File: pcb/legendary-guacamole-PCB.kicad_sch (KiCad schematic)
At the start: 2 parts

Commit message: forget to commit
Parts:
- added U1: nRF52840, Package_DFN_QFN:Nordic_AQFN-73-1EP_7x7mm_P0.5mm, symbol MCU_Nordic:nRF52840
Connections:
- new net: U1.A22 (VDD), U1.AD14 (VDD), U1.AD23 (VDD), U1.B1 (VDD), U1.W1 (VDD)
- new net: U1.B7 (VSS), U1.EP (VSS)
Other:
- note removed: "Columns"
- note removed: "Rows"

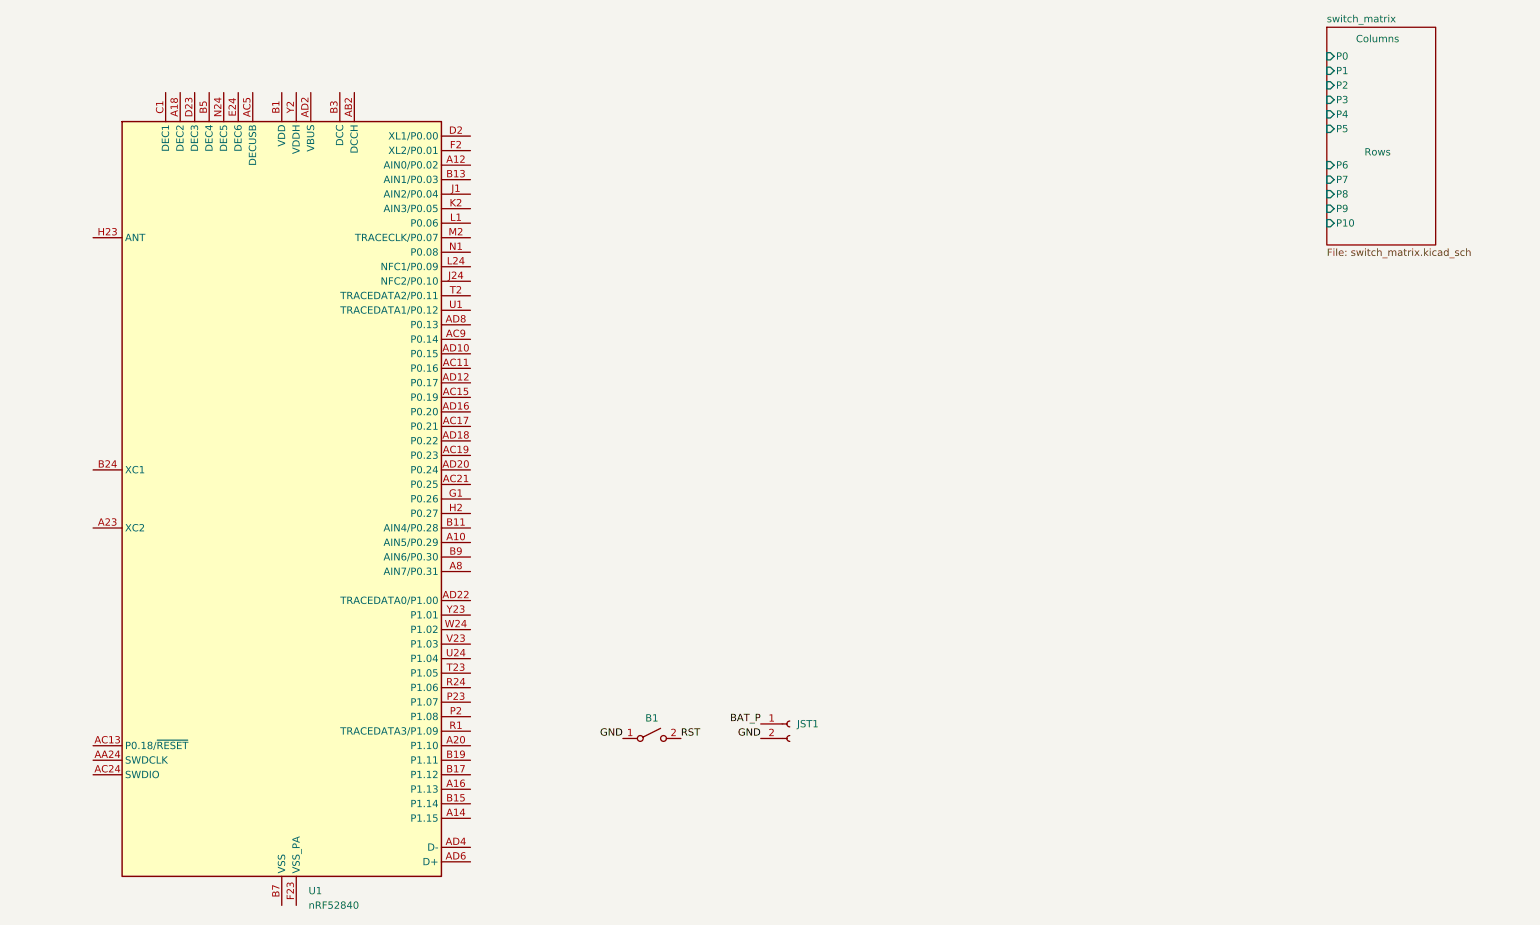
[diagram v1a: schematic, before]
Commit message: fix diff between updated pcb and schematic
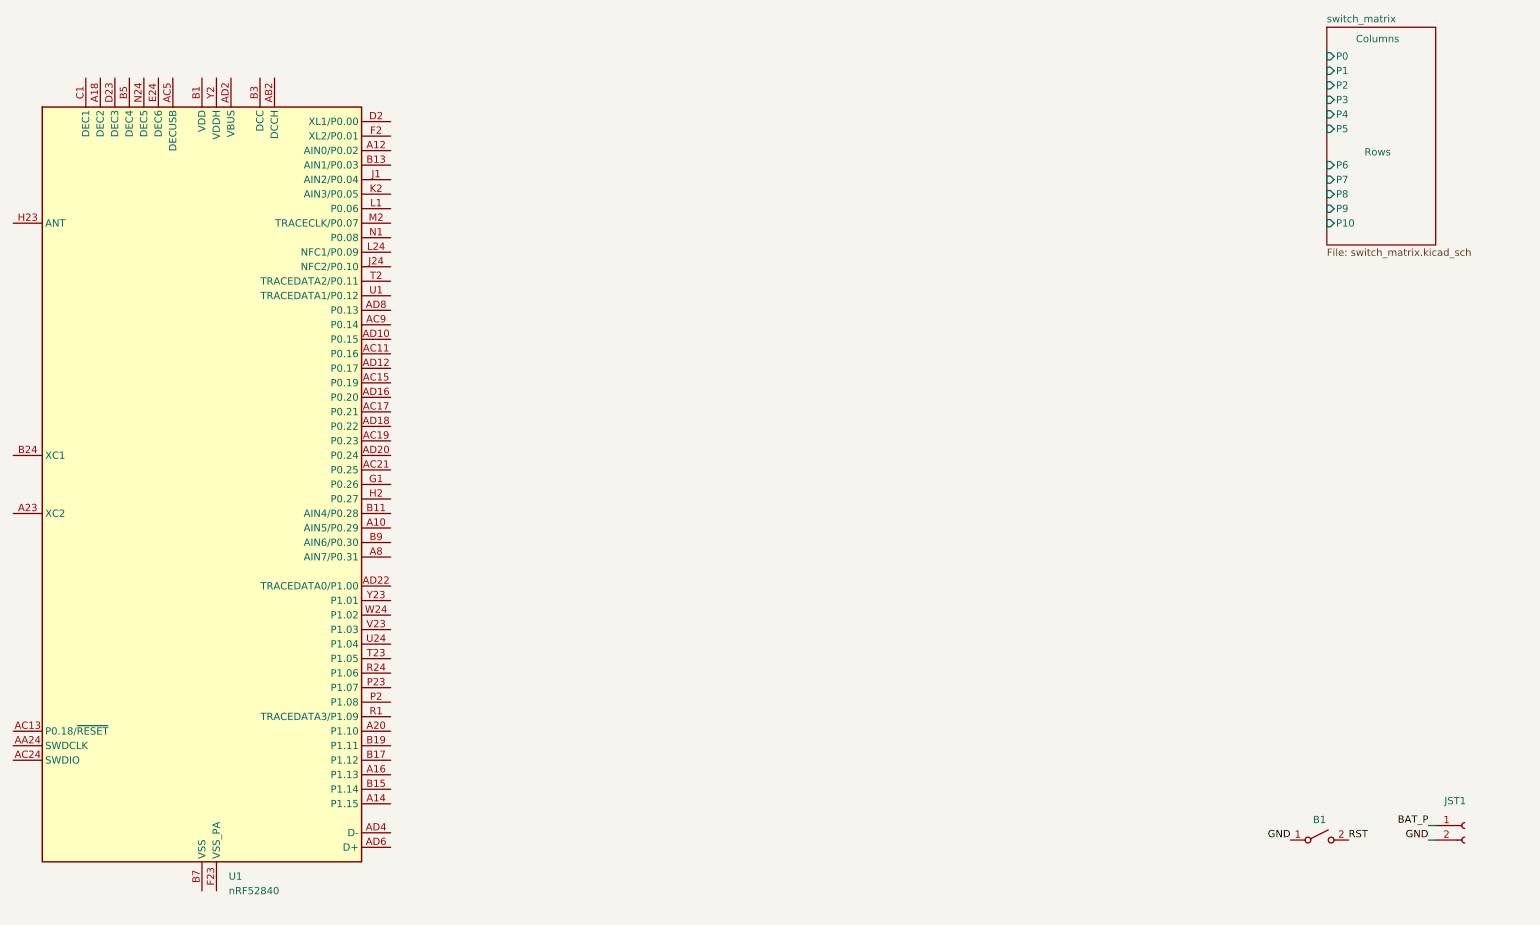
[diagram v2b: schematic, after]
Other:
- moved on the sheet: B1, JST1, U1

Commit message: finish pcb routing, generate fabrication file and bom
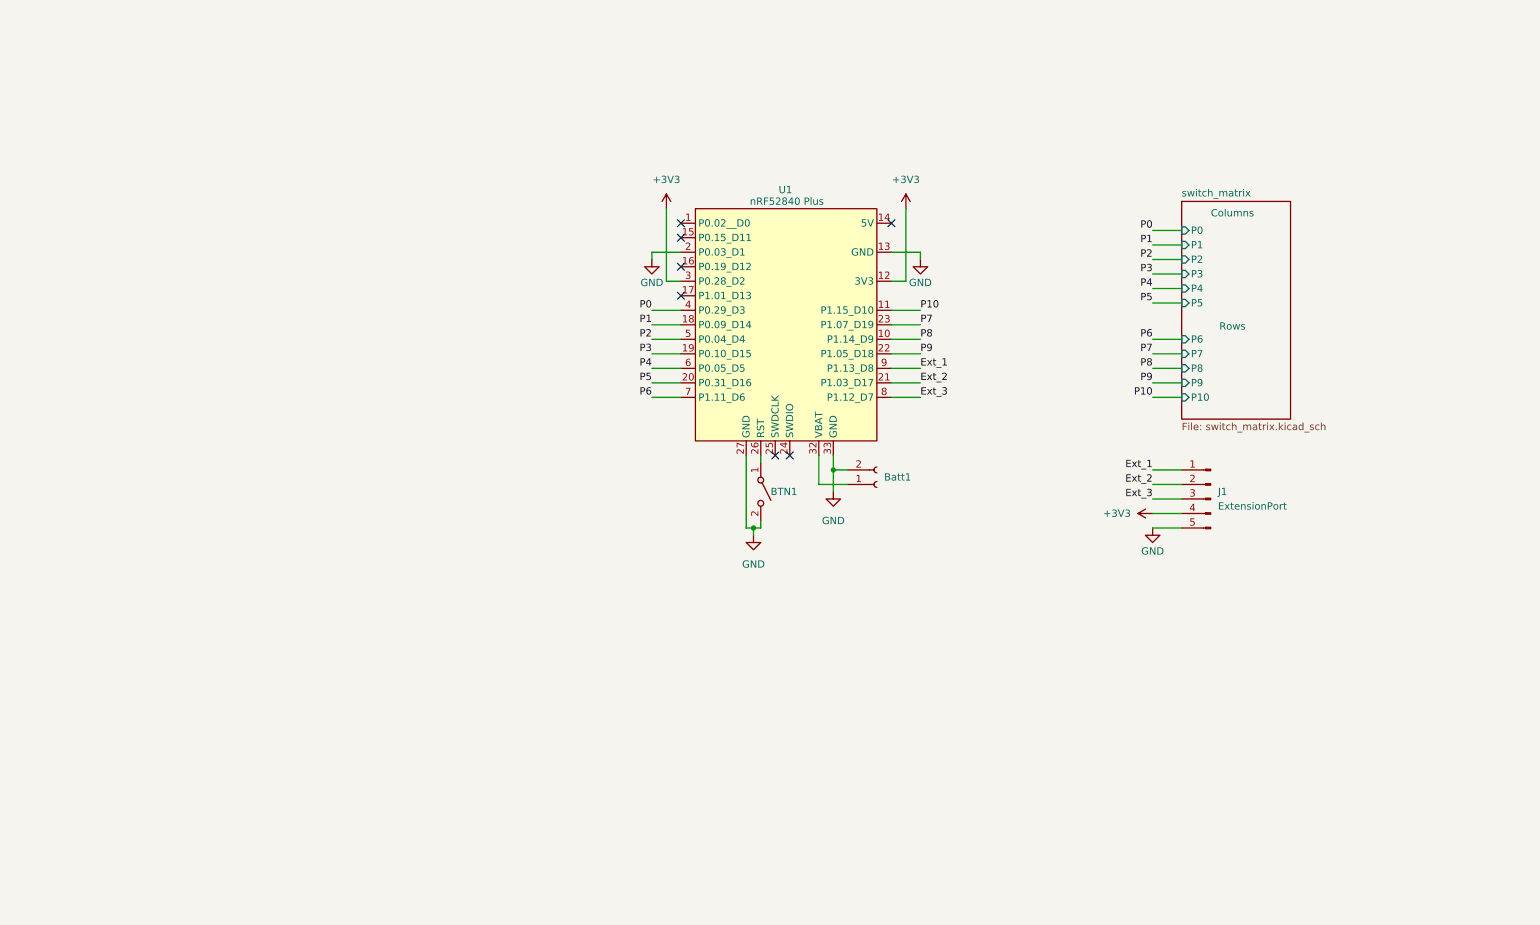
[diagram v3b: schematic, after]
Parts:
- removed U1: nRF52840, Package_DFN_QFN:Nordic_AQFN-73-1EP_7x7mm_P0.5mm, symbol MCU_Nordic:nRF52840
- added J1: ExtensionPort, Connector_PinHeader_2.54mm:PinHeader_1x05_P2.54mm_Vertical, symbol Connector:Conn_01x05_Pin
- added U1: nRF52840 Plus, library:XIAO-nRF52840-Plus-SMD, symbol Seeed_Studio_XIAO_Series:XIAO-nRF52840_Plus_SMD
- BTN1: renamed from B1; value ~ -> EVPBT5A4A000; footprint E73:SW_TACT_ALPS_SKQGABE010 -> library:EVPBT5A4A000
- renumbered JST1 to Batt1
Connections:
- net RST is gone; now on net GND: BTN1.2 (B)
- net GND: now also J1.5 (Pin_5), U1.13 (GND), U1.2 (P0.03_D1), U1.27 (GND), U1.33 (GND); no longer BTN1.1 (A)
- net BAT_P: no longer names the net of Batt1.1 (Pin_1)
- net BAT_P: now also U1.32 (VBAT)
- new net: BTN1.1 (A), U1.26 (RST)
- new net +3V3: J1.4 (Pin_4), U1.12 (3V3), U1.3 (P0.28_D2)
- new net Ext_1: J1.1 (Pin_1), U1.9 (P1.13_D8)
- new net Ext_2: J1.2 (Pin_2), U1.21 (P1.03_D17)
- new net Ext_3: J1.3 (Pin_3), U1.8 (P1.12_D7)
- new net P0: U1.4 (P0.29_D3)
- new net P1: U1.18 (P0.09_D14)
- new net P10: U1.11 (P1.15_D10)
- new net P2: U1.5 (P0.04_D4)
- new net P3: U1.19 (P0.10_D15)
- new net P4: U1.6 (P0.05_D5)
- new net P5: U1.20 (P0.31_D16)
- new net P6: U1.7 (P1.11_D6)
- new net P7: U1.23 (P1.07_D19)
- new net P8: U1.10 (P1.14_D9)
- new net P9: U1.22 (P1.05_D18)
- no-connect marks 0 -> 7
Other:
- moved on the sheet: BTN1, Batt1
